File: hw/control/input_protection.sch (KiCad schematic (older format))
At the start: 0 parts

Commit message: [hw] Sketch the input protection
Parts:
- added C?: C, symbol Device:C
- added D?: SD24_SOD323, Diode_SMD:D_SOD-323, symbol Diode:SD24_SOD323
- added D?: D_Zener, symbol Device:D_Zener
- added Q?: AOSP21357 ???, symbol my:Q_PMOS_SSSGDDDD
- added R?: 10K, symbol Device:R
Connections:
- wire segments 0 -> 30
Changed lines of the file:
@@
 Comment4 ""
 $EndDescr
-Text HLabel 5000 3500 0    50   Input ~ 0
+Text HLabel 3500 3500 0    50   Input ~ 0
 V_A
-Text HLabel 5000 4000 0    50   Input ~ 0
+Text HLabel 3450 4500 0    50   Input ~ 0
 V_B
 Text HLabel 6500 3500 2    50   Output ~ 0
 VOUT
-Text HLabel 6500 4000 2    50   Output ~ 0
+Text HLabel 6500 4500 2    50   Output ~ 0
 GND
+Wire Wire Line
+	3450 4500 3750 4500
+$Comp
+L my:Q_PMOS_SSSGDDDD Q?
+U 1 1 614E912B
+P 5150 3600
+F 0 "Q?" V 5775 3600 50  0000 C CNN
+F 1 "AOSP21357 ???" V 5684 3600 50  0000 C CNN
+F 2 "" H 5350 3700 50  0001 C CNN
+F 3 "~" H 5150 3600 50  0001 C CNN
+	1    5150 3600
+	0    -1   -1   0
+$EndComp
+Wire Wire Line
+	3500 3500 3750 3500
+Wire Wire Line
+	4850 3500 4850 3400
+Wire Wire Line
+	4850 3400 4950 3400
+Connection ~ 4850 3500
+Wire Wire Line
+	4850 3500 4950 3500
+Wire Wire Line
+	4850 3400 4850 3300
+Wire Wire Line
+	4850 3300 4950 3300
+Connection ~ 4850 3400
+Wire Wire Line
+	4850 3300 4850 3200
+Wire Wire Line
+	4850 3200 4950 3200
+Connection ~ 4850 3300
+Wire Wire Line
+	5350 3500 5450 3500
+Wire Wire Line
+	5450 3500 5450 3400
+Wire Wire Line
+	5450 3400 5350 3400
+Connection ~ 5450 3500
+Wire Wire Line
+	5450 3500 5650 3500
+Wire Wire Line
+	5450 3400 5450 3300
+Wire Wire Line
+	5450 3300 5350 3300
+Connection ~ 5450 3400
+$Comp
+L Device:R R?
+U 1 1 614EC7F7
+P 5150 4200
+F 0 "R?" H 5220 4246 50  0000 L CNN
+F 1 "10K" H 5220 4155 50  0000 L CNN
+F 2 "" V 5080 4200 50  0001 C CNN
+F 3 "~" H 5150 4200 50  0001 C CNN
+	1    5150 4200
+	1    0    0    -1
+$EndComp
+Wire Wire Line
+	5150 4350 5150 4500
+Connection ~ 5150 4500
+Wire Wire Line
+	5150 4500 6500 4500
+Wire Wire Line
+	5150 4050 5150 3900
+$Comp
+L Device:D_Zener D?
+U 1 1 614ED589
+P 5650 3750
+F 0 "D?" V 5604 3830 50  0000 L CNN
+F 1 "D_Zener" V 5695 3830 50  0000 L CNN
+F 2 "" H 5650 3750 50  0001 C CNN
+F 3 "~" H 5650 3750 50  0001 C CNN
+	1    5650 3750
+	0    1    1    0
+$EndComp
+Wire Wire Line
+	5650 3900 5150 3900
+Connection ~ 5150 3900
+Wire Wire Line
+	5150 3900 5150 3750
+Wire Wire Line
+	5650 3600 5650 3500
+Connection ~ 5650 3500
+Wire Wire Line
+	5650 3500 6500 3500
+$Comp
+L Diode:SD24_SOD323 D?
+U 1 1 61462F0A
+P 3750 3950
+F 0 "D?" V 3704 4029 50  0000 L CNN
+F 1 "SD24_SOD323" V 3795 4029 50  0000 L CNN
+F 2 "Diode_SMD:D_SOD-323" H 3750 3750 50  0001 C CNN
+F 3 "https://www.littelfuse.com/~/media/electronics/datasheets/tvs_diode_arrays/littelfuse_tvs_diode_array_sd_c_datasheet.pdf.pdf" H 3750 3950 50  0001 C CNN
+	1    3750 3950
+	0    1    1    0
+$EndComp
+Wire Wire Line
+	3750 3800 3750 3500
+Connection ~ 3750 3500
+Wire Wire Line
+	3750 3500 4550 3500
+Wire Wire Line
+	3750 4100 3750 4500
+Connection ~ 3750 4500
+Wire Wire Line
+	3750 4500 4550 4500
+$Comp
+L Device:C C?
+U 1 1 61464907
+P 4550 3950
+F 0 "C?" H 4665 3996 50  0000 L CNN
+F 1 "C" H 4665 3905 50  0000 L CNN
+F 2 "" H 4588 3800 50  0001 C CNN
+F 3 "~" H 4550 3950 50  0001 C CNN
+	1    4550 3950
+	1    0    0    -1
+$EndComp
+Wire Wire Line
+	4550 3500 4550 3800
+Connection ~ 4550 3500
+Wire Wire Line
+	4550 3500 4850 3500
+Wire Wire Line
+	4550 4100 4550 4500
+Connection ~ 4550 4500
+Wire Wire Line
+	4550 4500 5150 4500
 $EndSCHEMATC

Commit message: [hw] Add annotations, minor fixes
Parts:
- removed D?: SD24_SOD323, Diode_SMD:D_SOD-323, symbol Diode:SD24_SOD323
- added D502: D_TVS, symbol Device:D_TVS
- gave numbers to parts that had none: 4
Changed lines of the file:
@@
 encoding utf-8
 Sheet 5 7
-Title ""
-Date ""
-Rev ""
-Comp ""
-Comment1 ""
+Title "WS2812 Controller"
+Date "2021-09-16"
+Rev "1"
+Comp "Stefan Misik"
+Comment1 "Input Protection"
 Comment2 ""
 Comment3 ""
@@
 	3450 4500 3750 4500
 $Comp
-L my:Q_PMOS_SSSGDDDD Q?
+L my:Q_PMOS_SSSGDDDD Q501
 U 1 1 614E912B
 P 5150 3600
-F 0 "Q?" V 5775 3600 50  0000 C CNN
+F 0 "Q501" V 5775 3600 50  0000 C CNN
 F 1 "AOSP21357 ???" V 5684 3600 50  0000 C CNN
 F 2 "" H 5350 3700 50  0001 C CNN
@@
 Connection ~ 5450 3400
 $Comp
-L Device:R R?
+L Device:R R501
 U 1 1 614EC7F7
 P 5150 4200
-F 0 "R?" H 5220 4246 50  0000 L CNN
+F 0 "R501" H 5220 4246 50  0000 L CNN
 F 1 "10K" H 5220 4155 50  0000 L CNN
 F 2 "" V 5080 4200 50  0001 C CNN
@@
 	5150 4050 5150 3900
 $Comp
-L Device:D_Zener D?
+L Device:D_Zener D501
 U 1 1 614ED589
 P 5650 3750
-F 0 "D?" V 5604 3830 50  0000 L CNN
+F 0 "D501" V 5604 3830 50  0000 L CNN
 F 1 "D_Zener" V 5695 3830 50  0000 L CNN
 F 2 "" H 5650 3750 50  0001 C CNN
@@
 Wire Wire Line
 	5650 3500 6500 3500
-$Comp
-L Diode:SD24_SOD323 D?
-U 1 1 61462F0A
-P 3750 3950
-F 0 "D?" V 3704 4029 50  0000 L CNN
-F 1 "SD24_SOD323" V 3795 4029 50  0000 L CNN
-F 2 "Diode_SMD:D_SOD-323" H 3750 3750 50  0001 C CNN
-F 3 "https://www.littelfuse.com/~/media/electronics/datasheets/tvs_diode_arrays/littelfuse_tvs_diode_array_sd_c_datasheet.pdf.pdf" H 3750 3950 50  0001 C CNN
-	1    3750 3950
-	0    1    1    0
-$EndComp
 Wire Wire Line
 	3750 3800 3750 3500
@@
 	3750 4500 4550 4500
 $Comp
-L Device:C C?
+L Device:C C501
 U 1 1 61464907
 P 4550 3950
-F 0 "C?" H 4665 3996 50  0000 L CNN
+F 0 "C501" H 4665 3996 50  0000 L CNN
 F 1 "C" H 4665 3905 50  0000 L CNN
 F 2 "" H 4588 3800 50  0001 C CNN
@@
 Wire Wire Line
 	4550 4500 5150 4500
+$Comp
+L Device:D_TVS D502
+U 1 1 6148FC75
+P 3750 3950
+F 0 "D502" V 3704 4030 50  0000 L CNN
+F 1 "D_TVS" V 3795 4030 50  0000 L CNN
+F 2 "" H 3750 3950 50  0001 C CNN
+F 3 "~" H 3750 3950 50  0001 C CNN
+	1    3750 3950
+	0    1    1    0
+$EndComp
 $EndSCHEMATC

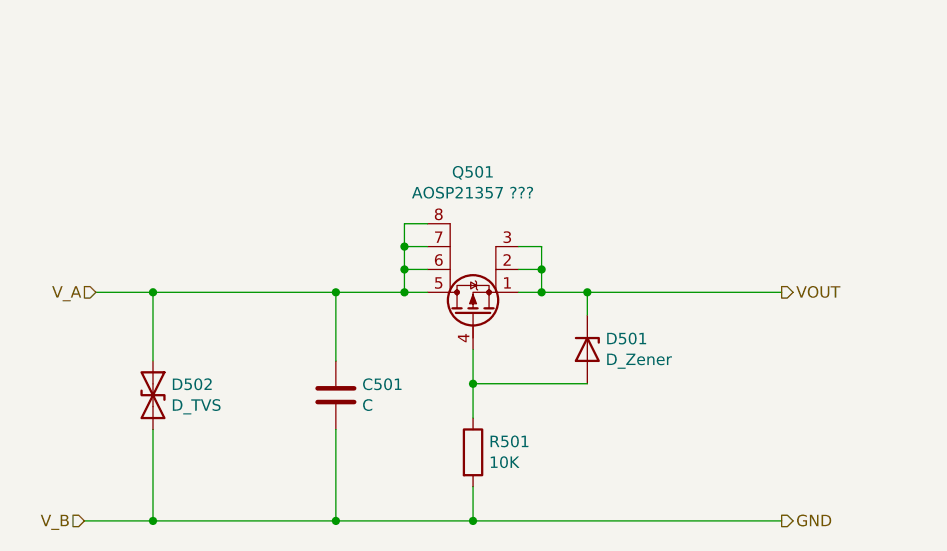
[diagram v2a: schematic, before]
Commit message: [hw] Add LED driver output sheets
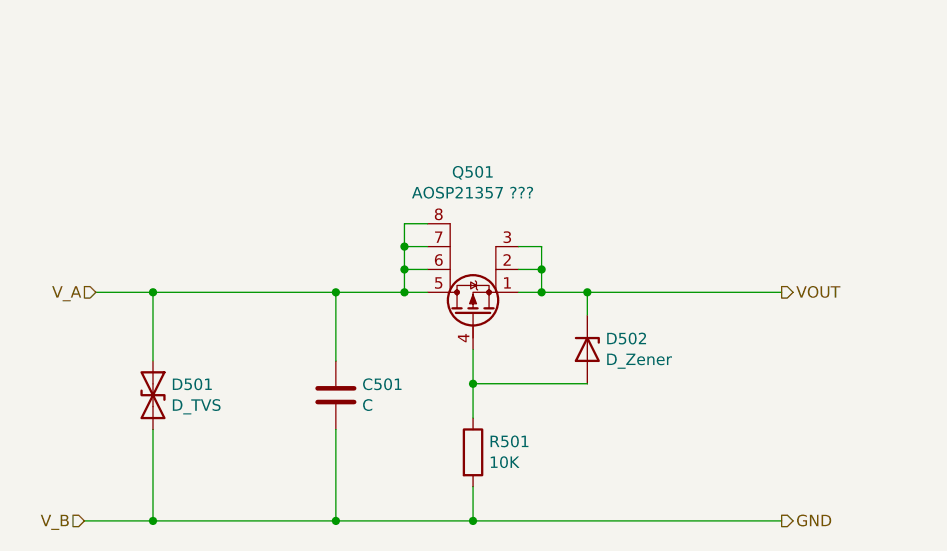
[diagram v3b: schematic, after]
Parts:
- renumbered D502 to D501, D501 to D502
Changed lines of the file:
@@
 $Descr A4 11693 8268
 encoding utf-8
-Sheet 5 7
+Sheet 5 9
 Title "WS2812 Controller"
-Date "2021-09-16"
+Date "2021-09-21"
 Rev "1"
 Comp "Stefan Misik"
@@
 	5150 4050 5150 3900
 $Comp
-L Device:D_Zener D501
+L Device:D_Zener D502
 U 1 1 614ED589
 P 5650 3750
-F 0 "D501" V 5604 3830 50  0000 L CNN
+F 0 "D502" V 5604 3830 50  0000 L CNN
 F 1 "D_Zener" V 5695 3830 50  0000 L CNN
 F 2 "" H 5650 3750 50  0001 C CNN
@@
 	4550 4500 5150 4500
 $Comp
-L Device:D_TVS D502
+L Device:D_TVS D501
 U 1 1 6148FC75
 P 3750 3950
-F 0 "D502" V 3704 4030 50  0000 L CNN
+F 0 "D501" V 3704 4030 50  0000 L CNN
 F 1 "D_TVS" V 3795 4030 50  0000 L CNN
 F 2 "" H 3750 3950 50  0001 C CNN

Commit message: [hw] Add some component types
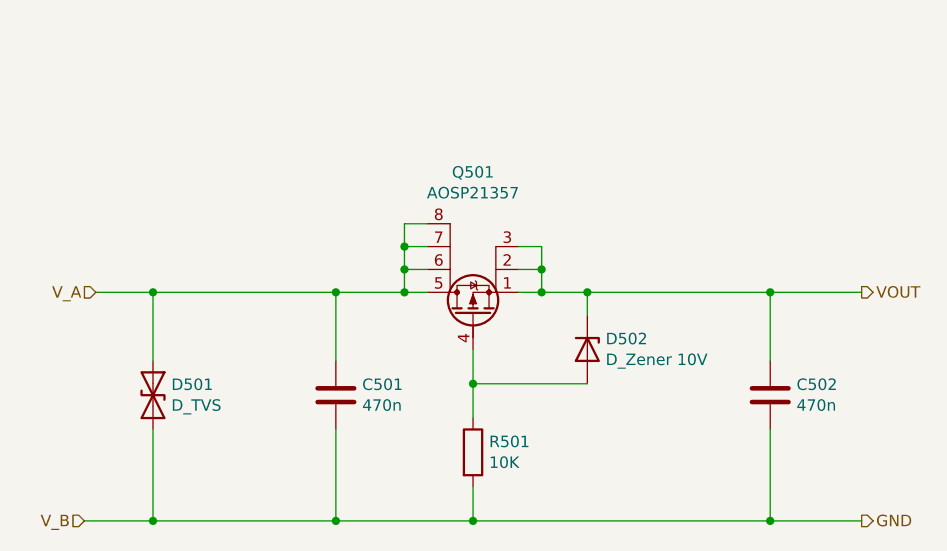
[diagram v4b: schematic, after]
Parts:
- added C502: 470n, symbol Device:C
- C501: value C -> 470n
- D502: value D_Zener -> D_Zener 10V
- Q501: value AOSP21357 ??? -> AOSP21357
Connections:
- net GND: now also C502.2
- net VOUT: now also C502.1
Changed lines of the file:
@@
 Text HLabel 3450 4500 0    50   Input ~ 0
 V_B
-Text HLabel 6500 3500 2    50   Output ~ 0
+Text HLabel 6850 3500 2    50   Output ~ 0
 VOUT
-Text HLabel 6500 4500 2    50   Output ~ 0
+Text HLabel 6850 4500 2    50   Output ~ 0
 GND
 Wire Wire Line
@@
 P 5150 3600
 F 0 "Q501" V 5775 3600 50  0000 C CNN
-F 1 "AOSP21357 ???" V 5684 3600 50  0000 C CNN
+F 1 "AOSP21357" V 5684 3600 50  0000 C CNN
 F 2 "" H 5350 3700 50  0001 C CNN
 F 3 "~" H 5150 3600 50  0001 C CNN
@@
 Connection ~ 5150 4500
 Wire Wire Line
-	5150 4500 6500 4500
+	5150 4500 6450 4500
 Wire Wire Line
 	5150 4050 5150 3900
@@
 P 5650 3750
 F 0 "D502" V 5604 3830 50  0000 L CNN
-F 1 "D_Zener" V 5695 3830 50  0000 L CNN
+F 1 "D_Zener 10V" V 5695 3830 50  0000 L CNN
 F 2 "" H 5650 3750 50  0001 C CNN
 F 3 "~" H 5650 3750 50  0001 C CNN
@@
 Connection ~ 5650 3500
 Wire Wire Line
-	5650 3500 6500 3500
+	5650 3500 6450 3500
 Wire Wire Line
 	3750 3800 3750 3500
@@
 Wire Wire Line
 	3750 4500 4550 4500
-$Comp
-L Device:C C501
-U 1 1 61464907
-P 4550 3950
-F 0 "C501" H 4665 3996 50  0000 L CNN
-F 1 "C" H 4665 3905 50  0000 L CNN
-F 2 "" H 4588 3800 50  0001 C CNN
-F 3 "~" H 4550 3950 50  0001 C CNN
-	1    4550 3950
-	1    0    0    -1
-$EndComp
 Wire Wire Line
 	4550 3500 4550 3800
@@
 	0    1    1    0
 $EndComp
+$Comp
+L Device:C C501
+U 1 1 61464907
+P 4550 3950
+F 0 "C501" H 4665 3996 50  0000 L CNN
+F 1 "470n" H 4665 3905 50  0000 L CNN
+F 2 "" H 4588 3800 50  0001 C CNN
+F 3 "~" H 4550 3950 50  0001 C CNN
+	1    4550 3950
+	1    0    0    -1
+$EndComp
+$Comp
+L Device:C C502
+U 1 1 6162C1F8
+P 6450 3950
+F 0 "C502" H 6565 3996 50  0000 L CNN
+F 1 "470n" H 6565 3905 50  0000 L CNN
+F 2 "" H 6488 3800 50  0001 C CNN
+F 3 "~" H 6450 3950 50  0001 C CNN
+	1    6450 3950
+	1    0    0    -1
+$EndComp
+Wire Wire Line
+	6450 3800 6450 3500
+Connection ~ 6450 3500
+Wire Wire Line
+	6450 3500 6850 3500
+Wire Wire Line
+	6450 4100 6450 4500
+Connection ~ 6450 4500
+Wire Wire Line
+	6450 4500 6850 4500
 $EndSCHEMATC

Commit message: [hw] Add some more peripherals
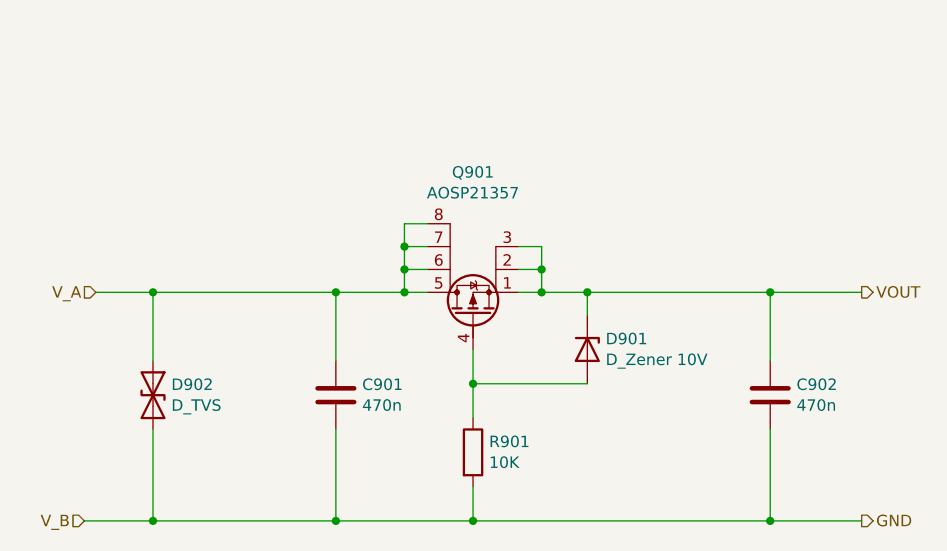
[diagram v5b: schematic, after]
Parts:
- renumbered C501 to C901, C502 to C902, D502 to D901, D501 to D902, Q501 to Q901, R501 to R901
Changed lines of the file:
@@
 $Descr A4 11693 8268
 encoding utf-8
-Sheet 5 9
+Sheet 9 13
 Title "WS2812 Controller"
-Date "2021-09-21"
+Date "2021-10-10"
 Rev "1"
 Comp "Stefan Misik"
@@
 	3450 4500 3750 4500
 $Comp
-L my:Q_PMOS_SSSGDDDD Q501
+L my:Q_PMOS_SSSGDDDD Q901
 U 1 1 614E912B
 P 5150 3600
-F 0 "Q501" V 5775 3600 50  0000 C CNN
+F 0 "Q901" V 5775 3600 50  0000 C CNN
 F 1 "AOSP21357" V 5684 3600 50  0000 C CNN
 F 2 "" H 5350 3700 50  0001 C CNN
@@
 Connection ~ 5450 3400
 $Comp
-L Device:R R501
+L Device:R R901
 U 1 1 614EC7F7
 P 5150 4200
-F 0 "R501" H 5220 4246 50  0000 L CNN
+F 0 "R901" H 5220 4246 50  0000 L CNN
 F 1 "10K" H 5220 4155 50  0000 L CNN
 F 2 "" V 5080 4200 50  0001 C CNN
@@
 	5150 4050 5150 3900
 $Comp
-L Device:D_Zener D502
+L Device:D_Zener D901
 U 1 1 614ED589
 P 5650 3750
-F 0 "D502" V 5604 3830 50  0000 L CNN
+F 0 "D901" V 5604 3830 50  0000 L CNN
 F 1 "D_Zener 10V" V 5695 3830 50  0000 L CNN
 F 2 "" H 5650 3750 50  0001 C CNN
@@
 	4550 4500 5150 4500
 $Comp
-L Device:D_TVS D501
+L Device:D_TVS D902
 U 1 1 6148FC75
 P 3750 3950
-F 0 "D501" V 3704 4030 50  0000 L CNN
+F 0 "D902" V 3704 4030 50  0000 L CNN
 F 1 "D_TVS" V 3795 4030 50  0000 L CNN
 F 2 "" H 3750 3950 50  0001 C CNN
@@
 $EndComp
 $Comp
-L Device:C C501
+L Device:C C901
 U 1 1 61464907
 P 4550 3950
-F 0 "C501" H 4665 3996 50  0000 L CNN
+F 0 "C901" H 4665 3996 50  0000 L CNN
 F 1 "470n" H 4665 3905 50  0000 L CNN
 F 2 "" H 4588 3800 50  0001 C CNN
@@
 $EndComp
 $Comp
-L Device:C C502
+L Device:C C902
 U 1 1 6162C1F8
 P 6450 3950
-F 0 "C502" H 6565 3996 50  0000 L CNN
+F 0 "C902" H 6565 3996 50  0000 L CNN
 F 1 "470n" H 6565 3905 50  0000 L CNN
 F 2 "" H 6488 3800 50  0001 C CNN

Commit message: [hw] Assign most of the controller footprints
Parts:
- C901, C902: footprint (none) -> Capacitor_SMD:C_0805_2012Metric_Pad1.18x1.45mm_HandSolder
- D901: footprint (none) -> Diode_SMD:D_MiniMELF_Handsoldering
- D902: footprint (none) -> Diode_SMD:D_SMA_Handsoldering
- Q901: footprint (none) -> Package_SO:SOIC-8_3.9x4.9mm_P1.27mm
- R901: footprint (none) -> Resistor_SMD:R_0805_2012Metric_Pad1.20x1.40mm_HandSolder
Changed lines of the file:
@@
 F 0 "Q901" V 5775 3600 50  0000 C CNN
 F 1 "AOSP21357" V 5684 3600 50  0000 C CNN
-F 2 "" H 5350 3700 50  0001 C CNN
+F 2 "Package_SO:SOIC-8_3.9x4.9mm_P1.27mm" H 5350 3700 50  0001 C CNN
 F 3 "~" H 5150 3600 50  0001 C CNN
 	1    5150 3600
@@
 F 0 "R901" H 5220 4246 50  0000 L CNN
 F 1 "10K" H 5220 4155 50  0000 L CNN
-F 2 "" V 5080 4200 50  0001 C CNN
+F 2 "Resistor_SMD:R_0805_2012Metric_Pad1.20x1.40mm_HandSolder" V 5080 4200 50  0001 C CNN
 F 3 "~" H 5150 4200 50  0001 C CNN
 	1    5150 4200
@@
 F 0 "D901" V 5604 3830 50  0000 L CNN
 F 1 "D_Zener 10V" V 5695 3830 50  0000 L CNN
-F 2 "" H 5650 3750 50  0001 C CNN
+F 2 "Diode_SMD:D_MiniMELF_Handsoldering" H 5650 3750 50  0001 C CNN
 F 3 "~" H 5650 3750 50  0001 C CNN
 	1    5650 3750
@@
 F 0 "D902" V 3704 4030 50  0000 L CNN
 F 1 "D_TVS" V 3795 4030 50  0000 L CNN
-F 2 "" H 3750 3950 50  0001 C CNN
+F 2 "Diode_SMD:D_SMA_Handsoldering" H 3750 3950 50  0001 C CNN
 F 3 "~" H 3750 3950 50  0001 C CNN
 	1    3750 3950
@@
 F 0 "C901" H 4665 3996 50  0000 L CNN
 F 1 "470n" H 4665 3905 50  0000 L CNN
-F 2 "" H 4588 3800 50  0001 C CNN
+F 2 "Capacitor_SMD:C_0805_2012Metric_Pad1.18x1.45mm_HandSolder" H 4588 3800 50  0001 C CNN
 F 3 "~" H 4550 3950 50  0001 C CNN
 	1    4550 3950
@@
 F 0 "C902" H 6565 3996 50  0000 L CNN
 F 1 "470n" H 6565 3905 50  0000 L CNN
-F 2 "" H 6488 3800 50  0001 C CNN
+F 2 "Capacitor_SMD:C_0805_2012Metric_Pad1.18x1.45mm_HandSolder" H 6488 3800 50  0001 C CNN
 F 3 "~" H 6450 3950 50  0001 C CNN
 	1    6450 3950

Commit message: [hw] Assign control board footprints
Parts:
- D902: footprint Diode_SMD:D_SMA_Handsoldering -> Diode_SMD:D_SMB-SMC_Universal_Handsoldering
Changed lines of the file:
@@
 F 0 "D902" V 3704 4030 50  0000 L CNN
 F 1 "D_TVS" V 3795 4030 50  0000 L CNN
-F 2 "Diode_SMD:D_SMA_Handsoldering" H 3750 3950 50  0001 C CNN
+F 2 "Diode_SMD:D_SMB-SMC_Universal_Handsoldering" H 3750 3950 50  0001 C CNN
 F 3 "~" H 3750 3950 50  0001 C CNN
 	1    3750 3950

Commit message: [hw] Incorporate suggestions
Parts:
- added Q902: IRF9540N, Package_TO_SOT_THT:TO-220-3_Vertical, symbol Transistor_FET:IRF9540N
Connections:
- net VOUT: now also Q902.3 (S)
- net V_A: now also Q902.2 (D)
- net at D901.2 (A), Q901.4 (G), R901.1: now also Q902.1 (G)
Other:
- note added: "Alternative\nNot mounted"
- moved on the sheet: C901
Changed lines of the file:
@@
 Connection ~ 5450 3500
 Wire Wire Line
-	5450 3500 5650 3500
+	5450 3500 5550 3500
 Wire Wire Line
 	5450 3400 5450 3300
@@
 Connection ~ 5150 3900
 Wire Wire Line
-	5150 3900 5150 3750
+	5150 3900 5150 3800
 Wire Wire Line
 	5650 3600 5650 3500
@@
 Connection ~ 3750 3500
 Wire Wire Line
-	3750 3500 4550 3500
+	3750 3500 4200 3500
 Wire Wire Line
 	3750 4100 3750 4500
 Connection ~ 3750 4500
 Wire Wire Line
-	3750 4500 4550 4500
+	3750 4500 4200 4500
 Wire Wire Line
-	4550 3500 4550 3800
-Connection ~ 4550 3500
+	4200 3500 4200 3800
+Connection ~ 4200 3500
 Wire Wire Line
-	4550 3500 4850 3500
+	4200 3500 4300 3500
 Wire Wire Line
-	4550 4100 4550 4500
-Connection ~ 4550 4500
+	4200 4100 4200 4500
+Connection ~ 4200 4500
 Wire Wire Line
-	4550 4500 5150 4500
+	4200 4500 5150 4500
 $Comp
 L Device:D_TVS D902
@@
 L Device:C C901
 U 1 1 61464907
-P 4550 3950
-F 0 "C901" H 4665 3996 50  0000 L CNN
-F 1 "470n" H 4665 3905 50  0000 L CNN
-F 2 "Capacitor_SMD:C_0805_2012Metric_Pad1.18x1.45mm_HandSolder" H 4588 3800 50  0001 C CNN
-F 3 "~" H 4550 3950 50  0001 C CNN
-	1    4550 3950
+P 4200 3950
+F 0 "C901" H 4315 3996 50  0000 L CNN
+F 1 "470n" H 4315 3905 50  0000 L CNN
+F 2 "Capacitor_SMD:C_0805_2012Metric_Pad1.18x1.45mm_HandSolder" H 4238 3800 50  0001 C CNN
+F 3 "~" H 4200 3950 50  0001 C CNN
+	1    4200 3950
 	1    0    0    -1
 $EndComp
@@
 Wire Wire Line
 	6450 4500 6850 4500
+$Comp
+L Transistor_FET:IRF9540N Q902
+U 1 1 61697CC0
+P 4550 2800
+F 0 "Q902" V 4892 2800 50  0000 C CNN
+F 1 "IRF9540N" V 4801 2800 50  0000 C CNN
+F 2 "Package_TO_SOT_THT:TO-220-3_Vertical" H 4750 2725 50  0001 L CIN
+F 3 "http://www.irf.com/product-info/datasheets/data/irf9540n.pdf" H 4550 2800 50  0001 L CNN
+	1    4550 2800
+	0    -1   -1   0
+$EndComp
+Wire Wire Line
+	4550 3000 4550 3800
+Wire Wire Line
+	4550 3800 5150 3800
+Connection ~ 5150 3800
+Wire Wire Line
+	5150 3800 5150 3750
+Wire Wire Line
+	4350 2700 4300 2700
+Wire Wire Line
+	4300 2700 4300 3500
+Connection ~ 4300 3500
+Wire Wire Line
+	4300 3500 4850 3500
+Wire Wire Line
+	4750 2700 5550 2700
+Wire Wire Line
+	5550 2700 5550 3500
+Connection ~ 5550 3500
+Wire Wire Line
+	5550 3500 5650 3500
+Text Notes 3900 2500 0    50   ~ 0
+Alternative\nNot mounted
+Wire Notes Line
+	3850 3100 4850 3100
+Wire Notes Line
+	4850 3100 4850 2300
+Wire Notes Line
+	4850 2300 3850 2300
+Wire Notes Line
+	3850 2300 3850 3100
 $EndSCHEMATC
